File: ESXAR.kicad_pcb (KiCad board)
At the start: 2 copper layers, 71.1 x 58.9 mm, 44 parts, among them P1 ANALOG, P10 USB_A, P11 USB_B, P12 SERVO/INPUT, P13 ANALOG, P16 BREADBOARD_POWER, P17 SENSOR, P18 EXTIO, P19 UNIVERSAL, P2 BREADBOARD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

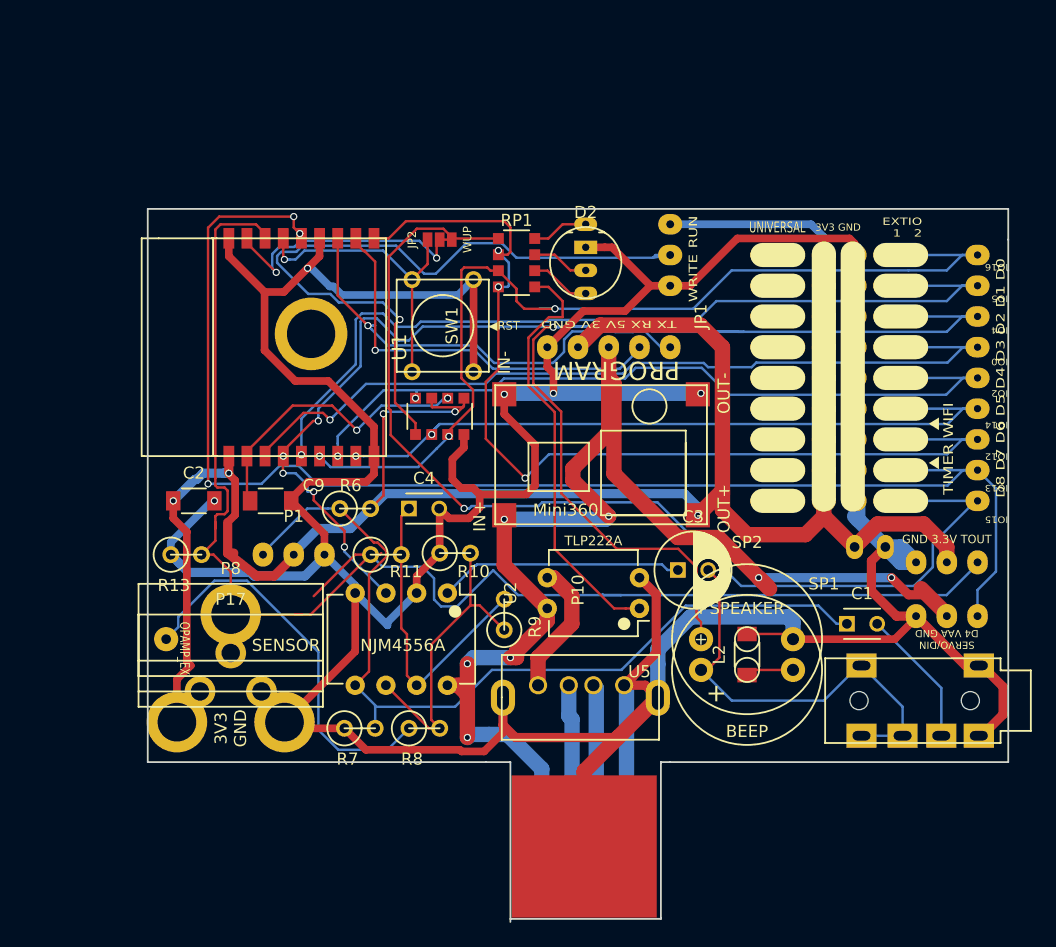
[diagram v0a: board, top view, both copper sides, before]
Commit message: Change IO Ext pin direction, and througehwole size.
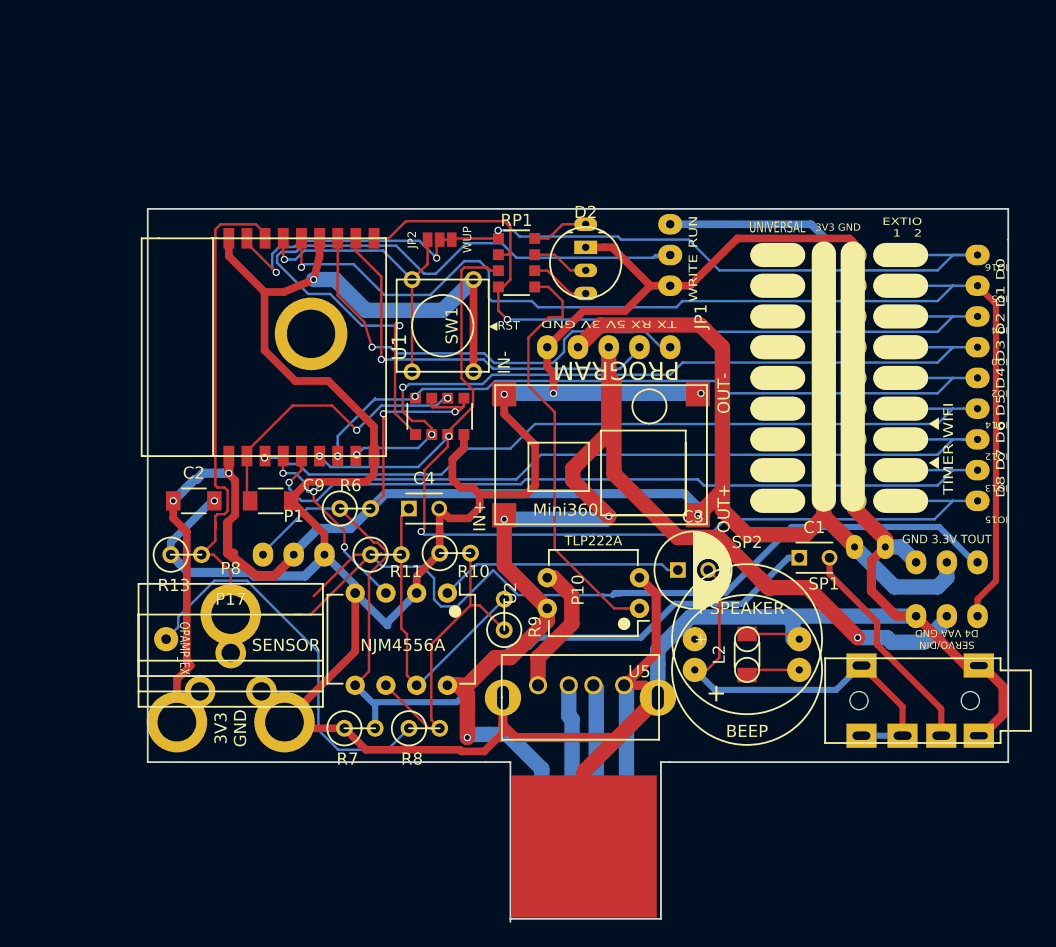
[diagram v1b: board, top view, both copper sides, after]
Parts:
- P18, P19, P20: footprint library:SolderWirePad_Oval_9xInline_0-6mmDrill -> library:SolderWirePad_Oval_9xInline_0-7mmDrill
- moved C1 6.73 mm to (191.0, 122.8)
- turned P18 to 270 degrees
- turned P2 to 270 degrees
- turned P5 to 270 degrees
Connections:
- P18 pad 7: Net-(P18-Pad7) -> Net-(JP3-Pad1)
- P2 pad 7: Net-(P18-Pad7) -> Net-(JP3-Pad1)
- P5 pad 7: Net-(P18-Pad7) -> Net-(JP3-Pad1)
- SP2 pad 1: Net-(P18-Pad7) -> Net-(JP3-Pad2)
- U1 pad 4: Net-(P18-Pad7) -> Net-(JP3-Pad1)
- U2 pad 3: Net-(P18-Pad7) -> Net-(JP3-Pad1)
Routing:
- net Net-(P18-Pad7): track 141.9 -> 0.00 mm, vias 6 -> 0
- net Net-(JP3-Pad1): track 0.00 -> 79.7 mm, vias 0 -> 3
- net Net-(JP2-Pad2): track 113.8 -> 76.6 mm
- net Net-(P12-Pad1): track 116.6 -> 98.4 mm, vias 3 -> 1
- net Net-(P18-Pad3): track 83.3 -> 67.1 mm, vias 3 -> 1
- net Net-(P18-Pad9): track 84.3 -> 92.7 mm
- net Net-(C1-Pad2): track 11.4 -> 18.7 mm
- net Net-(P18-Pad8): track 74.2 -> 67.5 mm
- net Net-(P18-Pad4): track 61.8 -> 67.0 mm, vias 2 -> 3
- net Net-(P18-Pad6): track 71.2 -> 67.5 mm
- net Net-(P18-Pad5): track 66.7 -> 63.4 mm
- net Net-(P13-Pad1): track 123.8 -> 127.0 mm
- net +5V: track 114.1 -> 111.5 mm, vias 7 -> 4
- net GND: track 374.6 -> 372.4 mm
- net Net-(C1-Pad1): track 72.9 -> 74.4 mm
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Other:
- board text added: "ESXAR Ver.20160802"
- board text removed: "ESXAR Ver.20160715"

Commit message: fix registor array bug
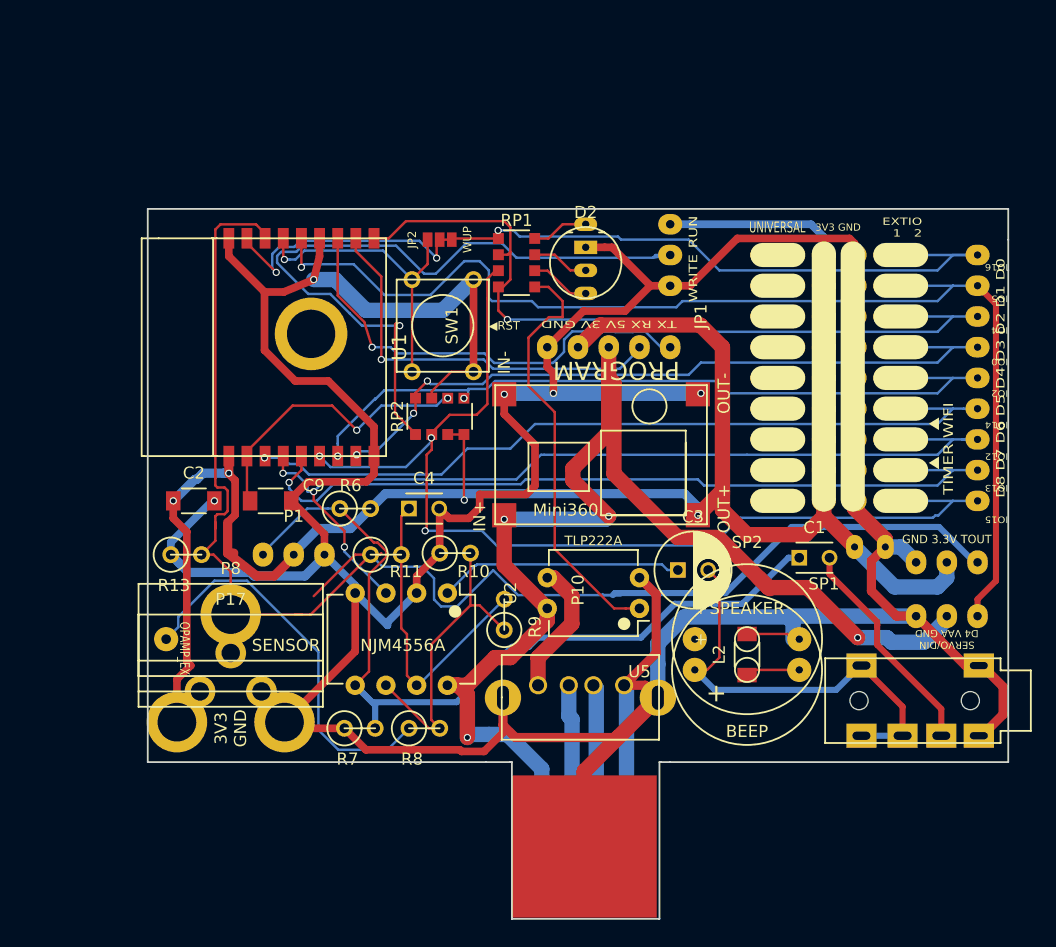
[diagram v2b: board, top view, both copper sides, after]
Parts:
- RP2: footprint Resistors_SMD:R_Array_Convex_4x1206 -> library:R_Array_For_R_Multi_library_4x1206
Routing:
- net +3V3: track 191.0 -> 179.9 mm, vias 6 -> 5
- net Net-(P18-Pad4): track 67.0 -> 62.0 mm
- net Net-(P18-Pad9): track 92.7 -> 90.0 mm
- net GND: track 372.4 -> 370.5 mm
- net Net-(P18-Pad5): track 63.4 -> 64.0 mm
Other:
- board size 71.1 x 58.9 mm -> 71.1 x 58.7 mm

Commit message: Ver 20160802. add speaker jumper,change analog port layout, etc.
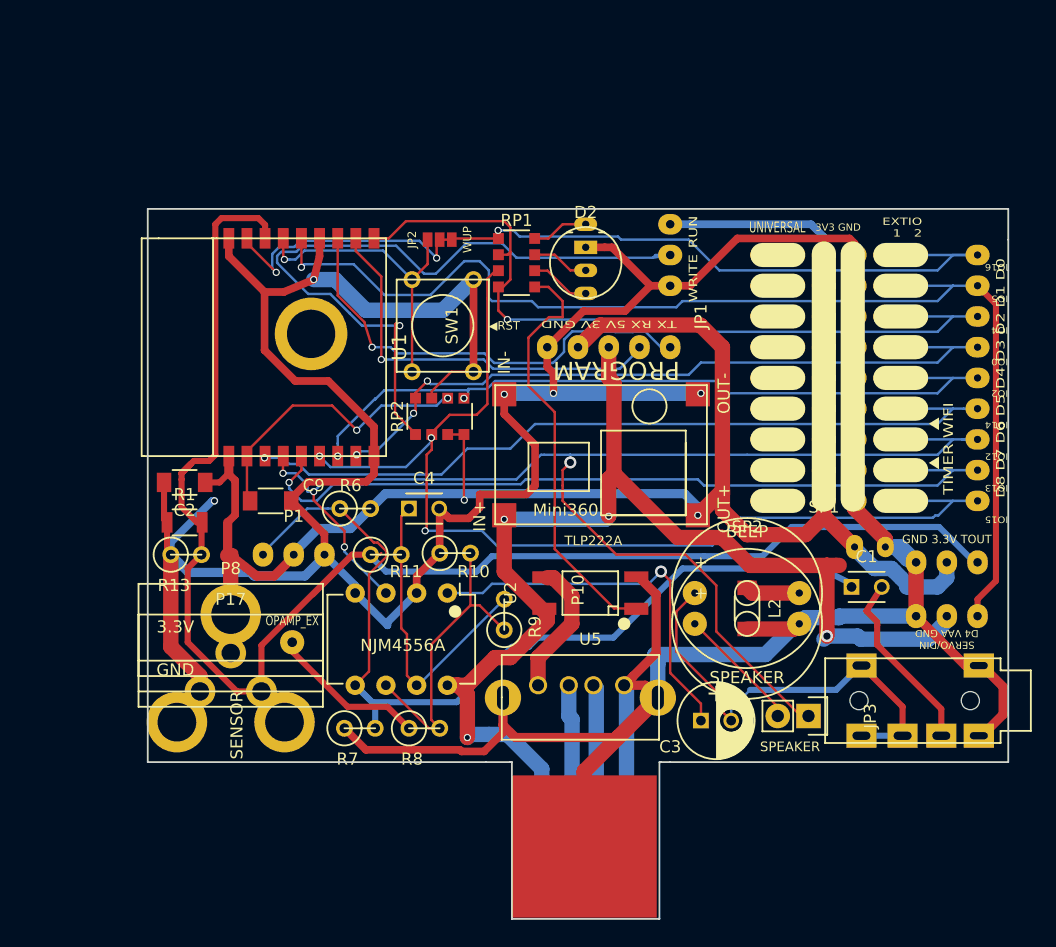
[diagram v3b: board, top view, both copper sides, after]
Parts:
- added JP3: JUMPER, Pin_Headers:Pin_Header_Straight_1x02, F.Cu at (191.8, 135.9)
- added R1: 4.7kΩ, Resistors_SMD:R_1206, F.Cu at (140.2, 119.9)
- U5: footprint Housings_DIP:DIP-4_W7.62mm -> Opto-Devices:Optocoupler_SMD_HandSoldering_KPC357_LTV35x_PC357_SingleChannel
- moved C3 12.6 mm to (182.9, 136.3)
- moved P4 10.4 mm to (149.1, 129.8)
- moved SP1 6.35 mm to (186.7, 125.7)
- moved C1 4.95 mm to (195.3, 125.2)
- moved U5 4.26 mm to (173.7, 125.7)
- moved L2 3.81 mm to (186.7, 127.0), turned to 270 degrees
- moved C2 1.70 mm to (140.2, 116.6), turned to 180 degrees
- moved SP2 1.27 mm to (186.7, 128.3)
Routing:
- net Net-(JP3-Pad1): track 79.7 -> 113.7 mm, vias 3 -> 4
- net Net-(P4-Pad1): track 32.9 -> 13.0 mm
- net +3V3: track 179.9 -> 162.5 mm, vias 5 -> 3
- net Net-(C3-Pad1): track 20.2 -> 32.1 mm, vias 1 -> 2
- net Net-(P13-Pad1): track 127.0 -> 138.5 mm
- net Net-(JP3-Pad2): track 0.00 -> 10.5 mm
- net +5V: track 111.5 -> 104.4 mm
- net Net-(C1-Pad1): track 74.4 -> 78.9 mm
- net Net-(C1-Pad2): track 18.7 -> 15.4 mm
- net GND: track 370.5 -> 372.5 mm
- net Net-(C3-Pad2): track 35.7 -> 37.1 mm
- net Net-(L2-Pad1): track 3.98 -> 4.83 mm
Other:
- board text added: "3.3V"
- board text added: "GND"
- board text added: "SPEAKER"

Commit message: Ver 20160804 Layout Change.
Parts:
- added C5: 100uF, Capacitors_ThroughHole:C_Radial_D6.3_L11.2_P2.5, F.Cu at (176.8, 125.9)
- added C6: 10uF, library:C_1206_HandSoldering_Small, F.Cu at (169.5, 111.7)
- added C7: 10uF, library:C_1206_HandSoldering_Small, F.Cu at (179.4, 107.7)
- added C8: 100uF, Capacitors_ThroughHole:C_Radial_D6.3_L11.2_P2.5, F.Cu at (169.3, 126.0)
- added L1: 4.7uH, library:C_1206_HandSoldering_Small, F.Cu at (177.4, 113.0)
- added SW2: DIN, Buttons_Switches_ThroughHole:SW_PUSH_SMALL, F.Cu at (161.3, 95.2)
- added U4: MT5201-3.3N, TO_SOT_Packages_SMD:SOT-23-5, F.Cu at (174.5, 109.5)
- added U7: LD1117CV33, Power_Integrations:TO-220, F.Cu at (170.2, 106.0)
- added U8: TA48M033F, TO_SOT_Packages_THT:SOT126_SOT32_Housing_Vertical_Mirrored, F.Cu at (177.8, 116.8)
- P11: moved to F.Cu
- moved U3 69.0 mm to (139.1, 127.0), turned to 0 degrees
- moved R1 62.6 mm to (202.7, 121.9)
- moved P8 59.9 mm to (203.9, 128.5), turned to 280 degrees
- moved P17 57.3 mm to (201.3, 128.9), turned to 280 degrees
- moved R13 57.2 mm to (197.5, 121.9)
- moved C1 51.5 mm to (144.7, 134.4)
- moved P4 44.6 mm to (193.7, 130.8)
- moved P13 39.9 mm to (179.1, 91.4)
- moved P12 39.0 mm to (188.6, 91.4)
- moved R11 35.9 mm to (191.0, 133.7), turned to 90 degrees
- moved P16 30.5 mm to (196.2, 91.4)
- moved JP3 30.3 mm to (161.5, 134.6)
- moved C3 28.3 mm to (154.6, 134.4), turned to 180 degrees
- moved R10 28.3 mm to (188.5, 133.7), turned to 90 degrees
- moved JP1 27.8 mm to (153.0, 92.7), turned to 0 degrees
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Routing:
- net +3V3: track 162.5 -> 217.9 mm, vias 3 -> 6
- net GND: track 372.5 -> 416.7 mm, vias 5 -> 10
- net Net-(JP1-Pad2): track 60.0 -> 26.3 mm, vias 1 -> 0
- net Net-(P13-Pad1): track 138.5 -> 121.3 mm, vias 0 -> 1
- net Net-(C3-Pad2): track 37.1 -> 23.6 mm
- net Net-(P12-Pad1): track 98.4 -> 111.5 mm
- net Net-(P18-Pad3): track 67.1 -> 79.1 mm, vias 1 -> 2
- net Net-(P3-Pad1): track 37.5 -> 29.0 mm, vias 1 -> 2
- net Net-(RP1-Pad5): track 35.1 -> 43.0 mm, vias 0 -> 2
- net Net-(R10-Pad2): track 25.7 -> 18.7 mm
- net Net-(P3-Pad2): track 33.8 -> 28.4 mm
- net +5V: track 104.4 -> 109.7 mm, vias 4 -> 3
- net Net-(D2-Pad1): track 4.70 -> 9.35 mm
- net Net-(P18-Pad5): track 64.0 -> 68.6 mm
- net Net-(L1-Pad1): track 0.00 -> 4.59 mm
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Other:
- board size 71.1 x 58.7 mm -> 71.1 x 60.6 mm
- board text added: "ANALOG"
- board text added: "BREADBOARD POWER▶"
- board text added: "ESXAR Ver.20160804"
- board text added: "GND 3.3V"
- board text added: "GPIO ▼ 16 5 4 0 2 14 12 13 15"
- board text added: "IN 3.3V GND"
- board text added: "IO16 IO5 IO4 IO0 IO2 IO14 IO12 IO13 IO15"
- board text added: "L8 L7 L6 L5 L4 L3 L2 L1 L0"
- board text added: "MODE"
- board text added: "SERVO/DIN D4 5V GND"
- board text added: "▲LUA/ NodeMCU"
- board text removed: "D0:IO16 D1:IO5 D2:IO4 D3:IO0 D4:IO2 D5:IO14 D6:IO12 D7:IO13 D8:IO15 D9:RX D10:TX"
- board text removed: "D8 D7 D6 D5 D4 D3 D2 D1 D0"
- board text removed: "ESXAR Ver.20160802"
- board text removed: "GND 3.3V TOUT"
- board text removed: "IO15 IO13 IO12 IO14 IO2 IO0 IO4 IO5 IO16"
- board text removed: "SERVO/DIN D4 VAA GND"

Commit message: Ver.20160805 change outline, rayout, delete opamp, etc...
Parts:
- removed C4: 0.1uF, Capacitors_ThroughHole:C_Disc_D3_P2.5
- removed P4: OPAMP EX, Wire_Pads:SolderWirePad_single_0-8mmDrill
- removed R10, R11, R6, R7, R8, R9: 4.7kΩ, Discret:R1
- removed U2: NJM4556A, Housings_DIP:DIP-8_W7.62mm
- JP1, P17, P8: moved to B.Cu
- moved OSHW 35.6 mm to (132.1, 97.2)
- moved C1 31.9 mm to (149.9, 102.9), turned to 90 degrees
- moved R1 31.0 mm to (172.1, 117.5)
- moved R13 26.5 mm to (172.1, 114.3)
- moved C7 25.4 mm to (159.4, 92.1), turned to 180 degrees
- moved U8 25.2 mm to (166.4, 94.4), turned to 270 degrees
- moved L1 22.7 mm to (163.2, 95.2), turned to 90 degrees
- moved P8 21.8 mm to (184.8, 118.1), turned to 90 degrees
- moved JP3 21.4 mm to (144.1, 122.2), turned to 0 degrees
- moved P17 21.3 mm to (182.2, 119.4), turned to 90 degrees
- moved P16 20.6 mm to (179.1, 80.0)
- moved U4 20.3 mm to (159.4, 95.9), turned to 90 degrees
- moved RP1 19.4 mm to (165.2, 82.9)
- moved P18 19.3 mm to (182.9, 99.1)
- moved P20 19.3 mm to (172.7, 99.1)
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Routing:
- net Net-(C1-Pad1): track 82.6 -> 24.6 mm
- net GND: track 416.7 -> 365.0 mm, vias 10 -> 3
- net Net-(JP3-Pad1): track 117.6 -> 81.2 mm, vias 4 -> 1
- net Net-(C3-Pad1): track 30.9 -> 0.00 mm
- net Net-(P12-Pad1): track 111.5 -> 85.3 mm, vias 1 -> 3
- net +3V3: track 217.9 -> 194.9 mm, vias 6 -> 7
- net Net-(C4-Pad1): track 22.5 -> 0.00 mm
- net Net-(P13-Pad1): track 121.3 -> 101.8 mm, vias 1 -> 2
- net Net-(C1-Pad2): track 11.7 -> 31.0 mm, vias 0 -> 2
- net Net-(R10-Pad2): track 18.7 -> 0.00 mm
- net +5V: track 109.7 -> 92.3 mm, vias 3 -> 1
- net Net-(P4-Pad1): track 13.2 -> 0.00 mm
- net Net-(P18-Pad3): track 79.1 -> 69.1 mm
- net Net-(RP1-Pad5): track 43.0 -> 34.4 mm
- net Net-(P18-Pad8): track 67.4 -> 58.9 mm
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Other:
- board size 71.1 x 60.6 mm -> 62.9 x 60.9 mm
- board text added: "D4 5V GND"
- board text added: "ESXAR Ver.20160805"
- board text added: "L8 L7 L6 l5 L4 L3 L2 L1 D0"
- board text added: "PROGRAM▼"
- board text added: "SERVO ◀/DIN"
- board text removed: "ESXAR Ver.20160804"
- board text removed: "PROGRAM"
- board text removed: "SERVO/DIN D4 5V GND"

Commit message: Ver.20170816  and documents
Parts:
- added P4: OPAMP EX, Wire_Pads:SolderWirePad_single_0-8mmDrill, F.Cu at (149.2, 122.6)
- moved SW1 9.53 mm to (151.8, 84.5)
- moved SW2 9.53 mm to (151.8, 94.0)
- moved U5 0.63 mm to (160.7, 109.9)
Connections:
- JP3 pad 2: Net-(JP3-Pad2) -> Net-(JP3-Pad1)
- SP2 pad 1: Net-(JP3-Pad2) -> Net-(JP3-Pad1)
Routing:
- net GND: track 365.0 -> 376.2 mm, vias 3 -> 4
- net Net-(JP3-Pad2): track 10.1 -> 0.00 mm
- net Net-(JP3-Pad1): track 81.2 -> 91.3 mm
- net Net-(C3-Pad1): track 0.00 -> 2.43 mm
- net +3V3: track 194.9 -> 196.6 mm
- net Net-(P10-Pad1): track 14.9 -> 16.1 mm
- net Net-(P13-Pad1): track 101.8 -> 100.5 mm
- net Net-(C3-Pad2): track 29.7 -> 30.2 mm
- net Net-(JP2-Pad1): track 25.5 -> 25.0 mm, vias 0 -> 1
- net Net-(P12-Pad1): track 85.3 -> 85.8 mm
- net +5V: track 92.3 -> 92.5 mm, vias 1 -> 0
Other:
- board text added: "16 5 4 0 2 14 12 13 15"
- board text added: "331"
- board text added: "472"
- board text added: "DIN▲"
- board text added: "ESXAR Ver.20160816"
- board text added: "GPIO▼"
- board text added: "L8 L7 L6 l5 L4 L3 L2 L1 L0"
- board text added: "LUA▲ /NodeMCU"
- board text added: "RESET▲"
- board text added: "▲BREADBOARD"
- board text added: "◀BREADBOARD POWER"
- board text removed: "ESXAR Ver.20160805"
- board text removed: "GPIO ▼ 16 5 4 0 2 14 12 13 15"
- board text removed: "L8 L7 L6 l5 L4 L3 L2 L1 D0"
- board text removed: "▲LUA/ NodeMCU"
- board text removed: "◀RST"
